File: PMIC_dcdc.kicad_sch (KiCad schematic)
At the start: 21 parts, among them U5 RK809-2

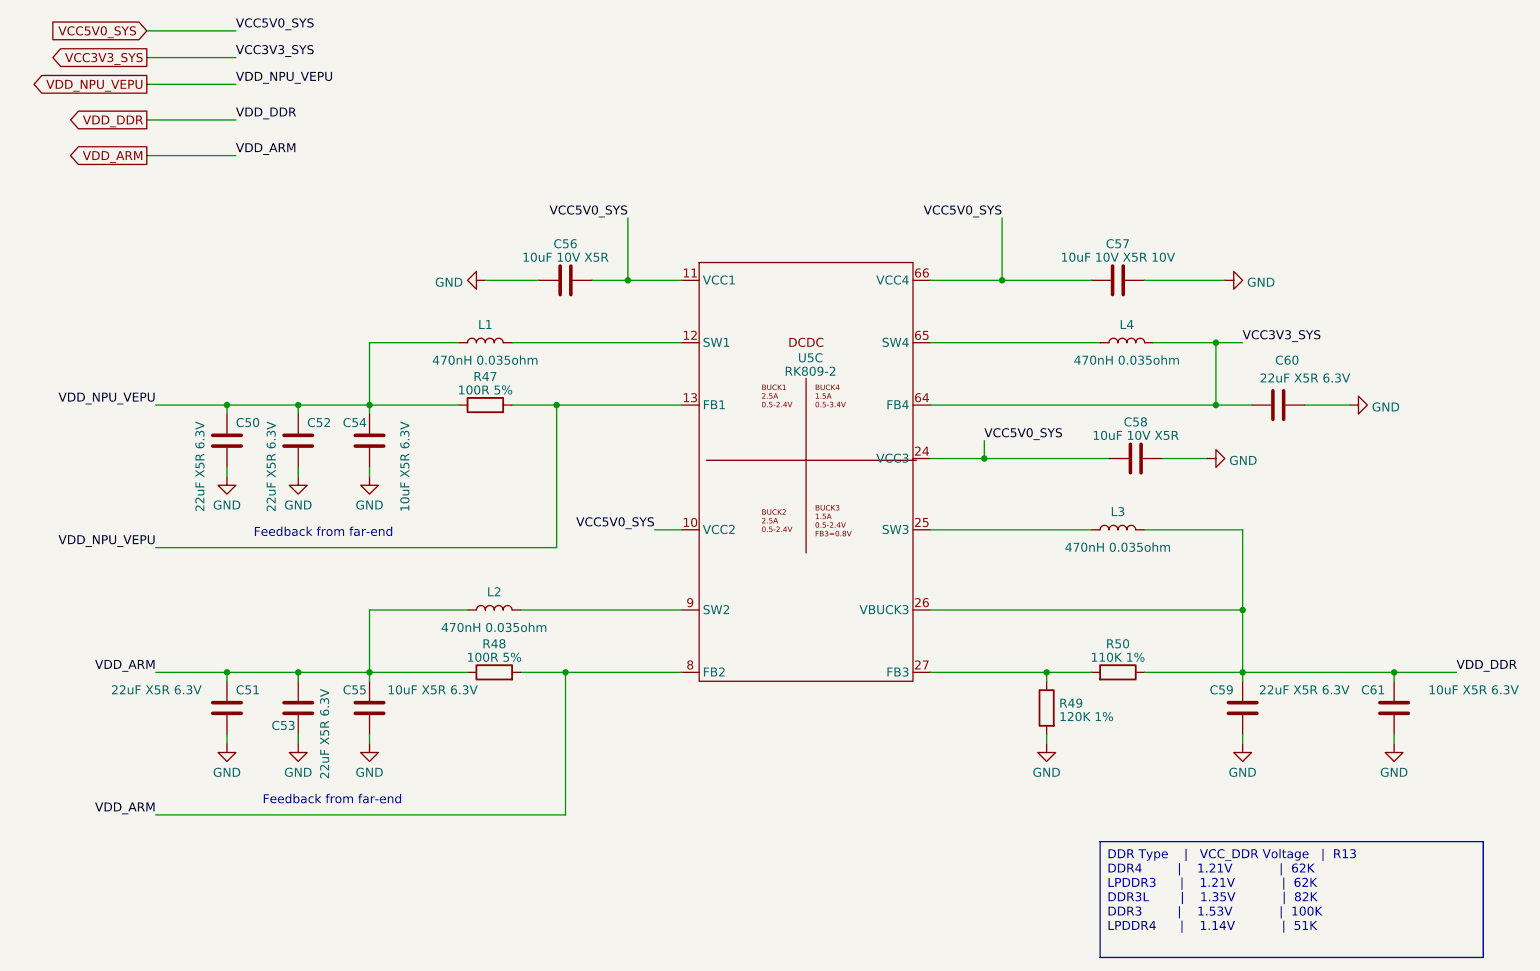
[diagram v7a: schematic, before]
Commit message: updated LCSC selection of capacitors
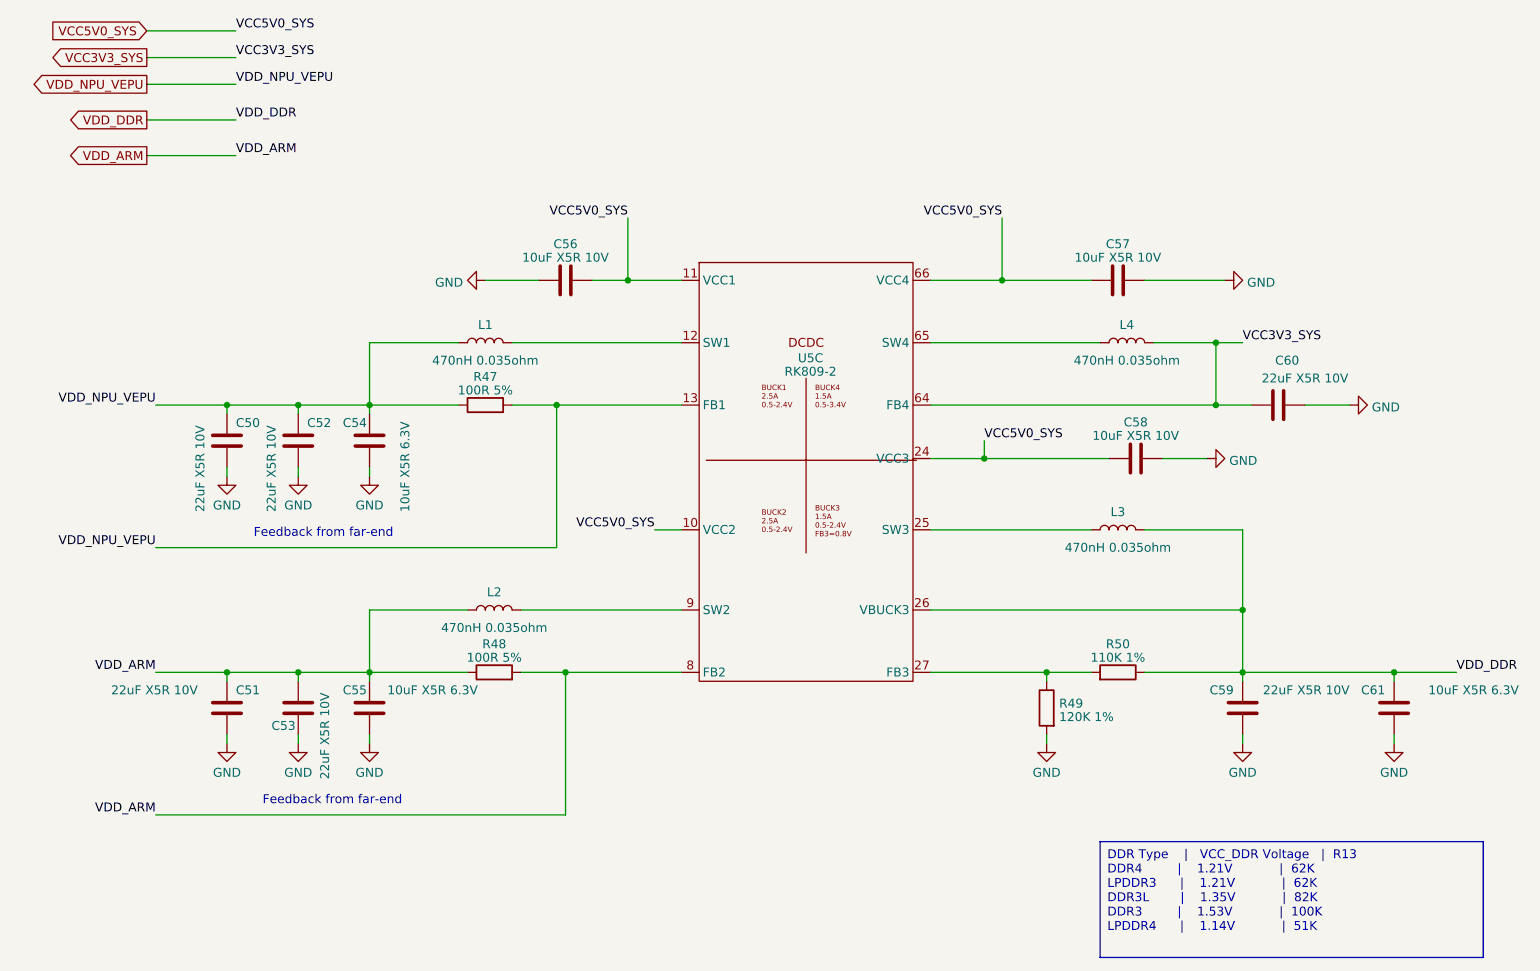
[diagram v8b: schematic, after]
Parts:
- C50, C51, C52, C53, C59: value 22uF X5R 6.3V -> 22uF X5R 10V; LCSC (none) -> C162690; Model (none) -> ZRB18AR61A226ME01L; Vendor (none) -> muRata(村田)
- C54, C55, C61: footprint Resistor_SMD:R_0603_1608Metric -> Resistor_SMD:R_0402_1005Metric; LCSC (none) -> C77000; Model (none) -> GRM155R61A106ME44D; Vendor (none) -> muRata(村田)
- C56: value 10uF 10V X5R -> 10uF X5R 10V; footprint (none) -> Capacitor_SMD:C_0402_1005Metric; LCSC (none) -> C77000; Model (none) -> GRM155R61A106ME44D; Vendor (none) -> muRata(村田)
- C57: value 10uF 10V X5R 10V -> 10uF X5R 10V; footprint Capacitor_SMD:C_0201_0603Metric -> Capacitor_SMD:C_0402_1005Metric; LCSC (none) -> C77000; Model (none) -> GRM155R61A106ME44D; Vendor (none) -> muRata(村田)
- C58: value 10uF 10V X5R -> 10uF X5R 10V; footprint Capacitor_SMD:C_0201_0603Metric -> Capacitor_SMD:C_0402_1005Metric; LCSC (none) -> C77000; Model (none) -> GRM155R61A106ME44D; Vendor (none) -> muRata(村田)
- C60: value 22uF X5R 6.3V -> 22uF X5R 10V; footprint Capacitor_SMD:C_0201_0603Metric -> Capacitor_SMD:C_0603_1608Metric; LCSC (none) -> C162690; Model (none) -> ZRB18AR61A226ME01L; Vendor (none) -> muRata(村田)
